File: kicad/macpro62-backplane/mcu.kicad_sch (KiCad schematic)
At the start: 0 parts

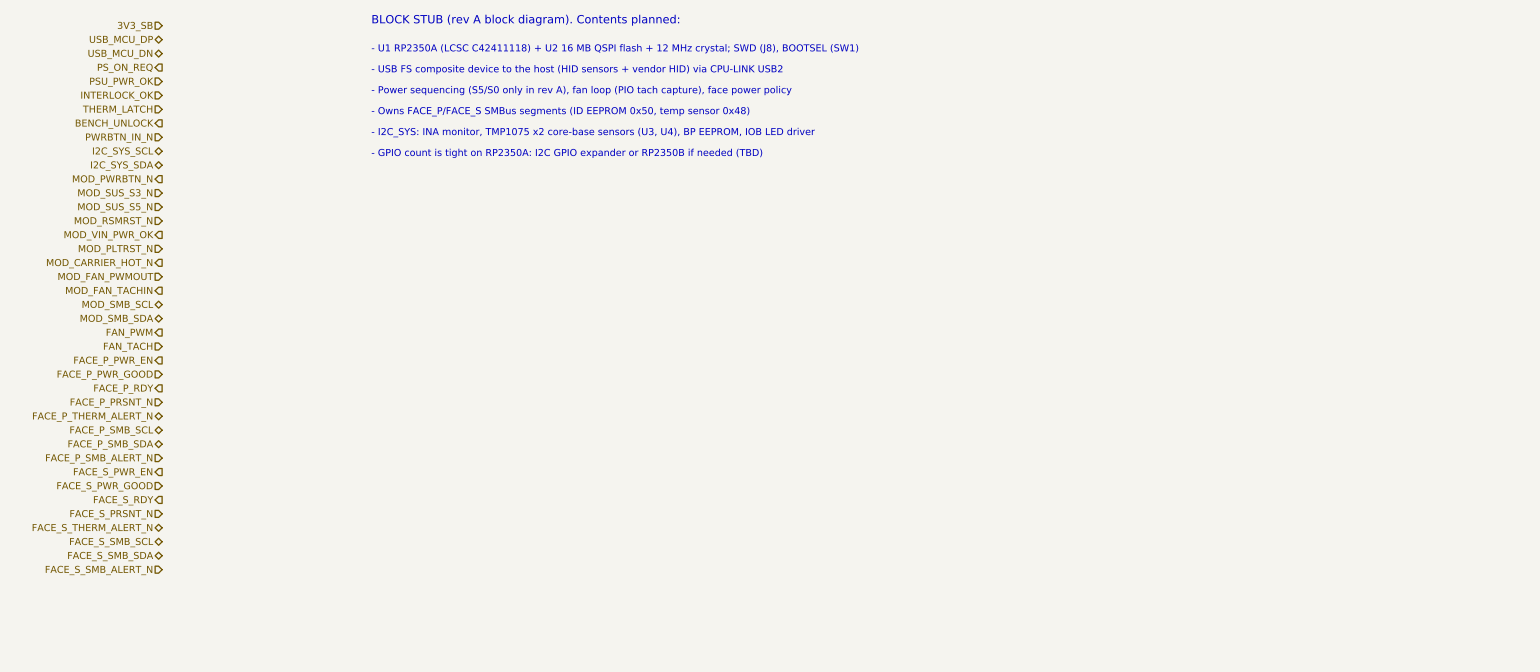
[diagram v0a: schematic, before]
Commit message: Cross-board compatibility audit: interface control doc, CR-BP-1 applied, J2/J3 row-swap pinouts, 15-pin face AUX, fan header removed from backplane, CPU board i226/BT1 cleanup
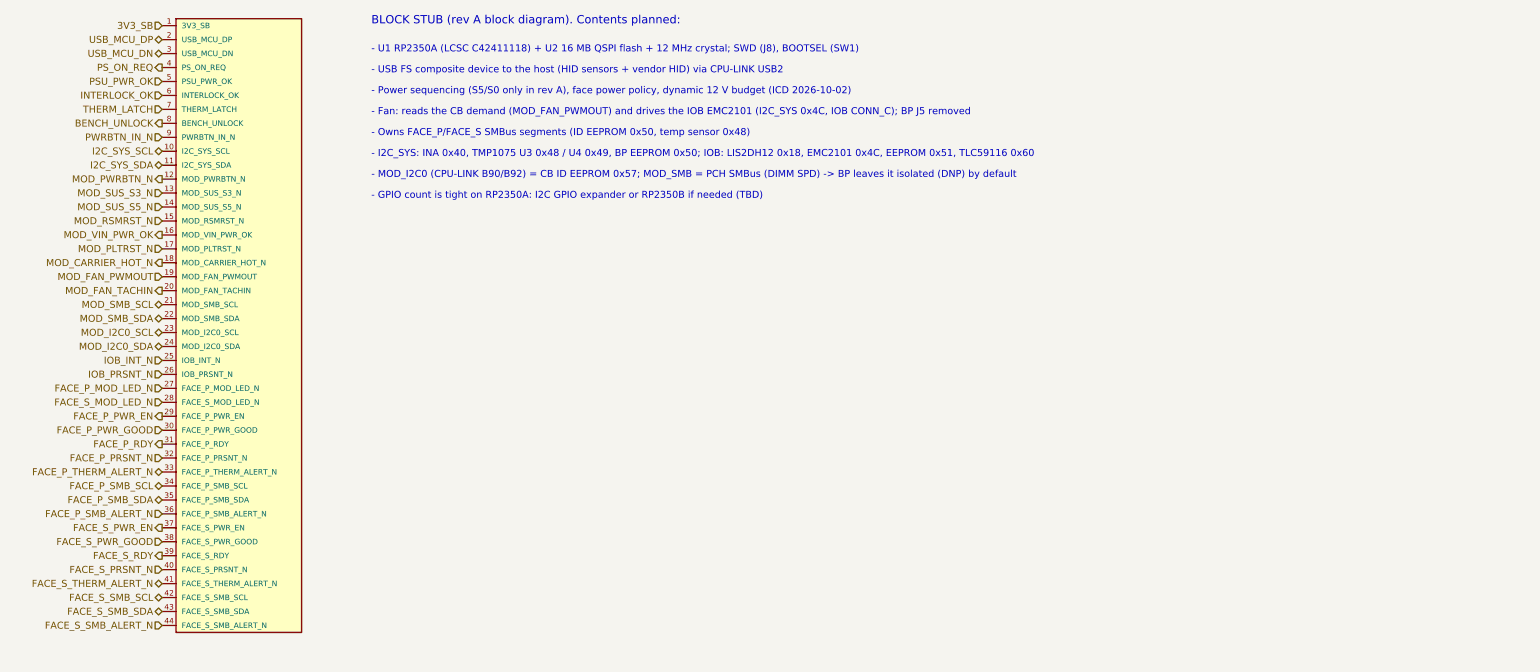
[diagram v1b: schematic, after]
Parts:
- added #BLK2: STUB_MCU, symbol MP62:STUB_MCU
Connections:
- net 3V3_SB: now also #BLK2.1 (3V3_SB)
- net BENCH_UNLOCK: now also #BLK2.8 (BENCH_UNLOCK)
- net FACE_P_PRSNT_N: now also #BLK2.32 (FACE_P_PRSNT_N)
- net FACE_P_PWR_EN: now also #BLK2.29 (FACE_P_PWR_EN)
- net FACE_P_PWR_GOOD: now also #BLK2.30 (FACE_P_PWR_GOOD)
- net FACE_P_RDY: now also #BLK2.31 (FACE_P_RDY)
- net FACE_P_SMB_ALERT_N: now also #BLK2.36 (FACE_P_SMB_ALERT_N)
- net FACE_P_SMB_SCL: now also #BLK2.34 (FACE_P_SMB_SCL)
- net FACE_P_SMB_SDA: now also #BLK2.35 (FACE_P_SMB_SDA)
- net FACE_P_THERM_ALERT_N: now also #BLK2.33 (FACE_P_THERM_ALERT_N)
- net FACE_S_PRSNT_N: now also #BLK2.40 (FACE_S_PRSNT_N)
- net FACE_S_PWR_EN: now also #BLK2.37 (FACE_S_PWR_EN)
- net FACE_S_PWR_GOOD: now also #BLK2.38 (FACE_S_PWR_GOOD)
- net FACE_S_RDY: now also #BLK2.39 (FACE_S_RDY)
- net FACE_S_SMB_ALERT_N: now also #BLK2.44 (FACE_S_SMB_ALERT_N)
- net FACE_S_SMB_SCL: now also #BLK2.42 (FACE_S_SMB_SCL)
- net FACE_S_SMB_SDA: now also #BLK2.43 (FACE_S_SMB_SDA)
- net FACE_S_THERM_ALERT_N: now also #BLK2.41 (FACE_S_THERM_ALERT_N)
- net I2C_SYS_SCL: now also #BLK2.10 (I2C_SYS_SCL)
- net I2C_SYS_SDA: now also #BLK2.11 (I2C_SYS_SDA)
- net INTERLOCK_OK: now also #BLK2.6 (INTERLOCK_OK)
- net MOD_CARRIER_HOT_N: now also #BLK2.18 (MOD_CARRIER_HOT_N)
- net MOD_FAN_PWMOUT: now also #BLK2.19 (MOD_FAN_PWMOUT)
- net MOD_FAN_TACHIN: now also #BLK2.20 (MOD_FAN_TACHIN)
- net MOD_PLTRST_N: now also #BLK2.17 (MOD_PLTRST_N)
- net MOD_PWRBTN_N: now also #BLK2.12 (MOD_PWRBTN_N)
- net MOD_RSMRST_N: now also #BLK2.15 (MOD_RSMRST_N)
- net MOD_SMB_SCL: now also #BLK2.21 (MOD_SMB_SCL)
- net MOD_SMB_SDA: now also #BLK2.22 (MOD_SMB_SDA)
- net MOD_SUS_S3_N: now also #BLK2.13 (MOD_SUS_S3_N)
- net MOD_SUS_S5_N: now also #BLK2.14 (MOD_SUS_S5_N)
- net MOD_VIN_PWR_OK: now also #BLK2.16 (MOD_VIN_PWR_OK)
- net PSU_PWR_OK: now also #BLK2.5 (PSU_PWR_OK)
- net PS_ON_REQ: now also #BLK2.4 (PS_ON_REQ)
- net PWRBTN_IN_N: now also #BLK2.9 (PWRBTN_IN_N)
- net THERM_LATCH: now also #BLK2.7 (THERM_LATCH)
- net USB_MCU_DN: now also #BLK2.3 (USB_MCU_DN)
- net USB_MCU_DP: now also #BLK2.2 (USB_MCU_DP)
- new net FACE_P_MOD_LED_N: #BLK2.27 (FACE_P_MOD_LED_N)
- new net FACE_S_MOD_LED_N: #BLK2.28 (FACE_S_MOD_LED_N)
- new net IOB_INT_N: #BLK2.25 (IOB_INT_N)
- new net IOB_PRSNT_N: #BLK2.26 (IOB_PRSNT_N)
- new net MOD_I2C0_SCL: #BLK2.23 (MOD_I2C0_SCL)
- new net MOD_I2C0_SDA: #BLK2.24 (MOD_I2C0_SDA)
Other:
- note added: "- Fan: reads the CB demand (MOD_FAN_PWMOUT) and drives the IOB EMC2101 (I2C_SYS 0x4C, IOB CONN_C); BP J5 removed"
- note added: "- I2C_SYS: INA 0x40, TMP1075 U3 0x48 / U4 0x49, BP EEPROM 0x50; IOB: LIS2DH12 0x18, EMC2101 0x4C, EEPROM 0x51, TLC59116 0x60"
- note added: "- MOD_I2C0 (CPU-LINK B90/B92) = CB ID EEPROM 0x57; MOD_SMB = PCH SMBus (DIMM SPD) -> BP leaves it isolated (DNP) by default"
- note added: "- Power sequencing (S5/S0 only in rev A), face power policy, dynamic 12 V budget (ICD 2026-10-02)"
- note removed: "- I2C_SYS: INA monitor, TMP1075 x2 core-base sensors (U3, U4), BP EEPROM, IOB LED driver"
- note removed: "- Power sequencing (S5/S0 only in rev A), fan loop (PIO tach capture), face power policy"
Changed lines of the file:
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@@
 	(title_block
 		(title "MP62 backplane: Management MCU (RP2350A)")
-		(date "2026-10-01")
-		(rev "A-bd1")
-		(comment 1 "Block stub: hierarchical labels only, circuit TBD")
+		(date "2026-10-02")
+		(rev "A-bd2")
+		(comment 1 "Block stub: hierarchical labels + one non-BOM stub symbol (#BLKn, passive pins) so ERC sees the nets; circuit TBD")
 	)
 	(hierarchical_label "3V3_SB"
@@
 		(effects (font (size 1.27 1.27)) (justify right))
 	)
-	(hierarchical_label "FAN_PWM"
-		(shape output)
+	(hierarchical_label "MOD_I2C0_SCL"
+		(shape bidirectional)
 		(at 38.1 86.36 180)
 		(effects (font (size 1.27 1.27)) (justify right))
 	)
-	(hierarchical_label "FAN_TACH"
-		(shape input)
+	(hierarchical_label "MOD_I2C0_SDA"
+		(shape bidirectional)
 		(at 38.1 88.90 180)
 		(effects (font (size 1.27 1.27)) (justify right))
 	)
+	(hierarchical_label "IOB_INT_N"
+		(shape input)
+		(at 38.1 91.44 180)
+		(effects (font (size 1.27 1.27)) (justify right))
+	)
+	(hierarchical_label "IOB_PRSNT_N"
+		(shape input)
+		(at 38.1 93.98 180)
+		(effects (font (size 1.27 1.27)) (justify right))
+	)
+	(hierarchical_label "FACE_P_MOD_LED_N"
+		(shape input)
+		(at 38.1 96.52 180)
+		(effects (font (size 1.27 1.27)) (justify right))
+	)
+	(hierarchical_label "FACE_S_MOD_LED_N"
+		(shape input)
+		(at 38.1 99.06 180)
+		(effects (font (size 1.27 1.27)) (justify right))
+	)
 	(hierarchical_label "FACE_P_PWR_EN"
 		(shape output)
-		(at 38.1 91.44 180)
+		(at 38.1 101.60 180)
 		(effects (font (size 1.27 1.27)) (justify right))
 	)
 	(hierarchical_label "FACE_P_PWR_GOOD"
 		(shape input)
-		(at 38.1 93.98 180)
+		(at 38.1 104.14 180)
 		(effects (font (size 1.27 1.27)) (justify right))
 	)
 	(hierarchical_label "FACE_P_RDY"
 		(shape output)
-		(at 38.1 96.52 180)
+		(at 38.1 106.68 180)
 		(effects (font (size 1.27 1.27)) (justify right))
 	)
 	(hierarchical_label "FACE_P_PRSNT_N"
 		(shape input)
-		(at 38.1 99.06 180)
+		(at 38.1 109.22 180)
 		(effects (font (size 1.27 1.27)) (justify right))
 	)
 	(hierarchical_label "FACE_P_THERM_ALERT_N"
 		(shape bidirectional)
-		(at 38.1 101.60 180)
+		(at 38.1 111.76 180)
 		(effects (font (size 1.27 1.27)) (justify right))
 	)
 	(hierarchical_label "FACE_P_SMB_SCL"
 		(shape bidirectional)
-		(at 38.1 104.14 180)
+		(at 38.1 114.30 180)
 		(effects (font (size 1.27 1.27)) (justify right))
 	)
 	(hierarchical_label "FACE_P_SMB_SDA"
 		(shape bidirectional)
-		(at 38.1 106.68 180)
+		(at 38.1 116.84 180)
 		(effects (font (size 1.27 1.27)) (justify right))
 	)
 	(hierarchical_label "FACE_P_SMB_ALERT_N"
 		(shape input)
-		(at 38.1 109.22 180)
+		(at 38.1 119.38 180)
 		(effects (font (size 1.27 1.27)) (justify right))
 	)
 	(hierarchical_label "FACE_S_PWR_EN"
 		(shape output)
-		(at 38.1 111.76 180)
+		(at 38.1 121.92 180)
 		(effects (font (size 1.27 1.27)) (justify right))
 	)
 	(hierarchical_label "FACE_S_PWR_GOOD"
 		(shape input)
-		(at 38.1 114.30 180)
+		(at 38.1 124.46 180)
 		(effects (font (size 1.27 1.27)) (justify right))
 	)
 	(hierarchical_label "FACE_S_RDY"
 		(shape output)
-		(at 38.1 116.84 180)
+		(at 38.1 127.00 180)
 		(effects (font (size 1.27 1.27)) (justify right))
 	)
 	(hierarchical_label "FACE_S_PRSNT_N"
 		(shape input)
-		(at 38.1 119.38 180)
+		(at 38.1 129.54 180)
 		(effects (font (size 1.27 1.27)) (justify right))
 	)
 	(hierarchical_label "FACE_S_THERM_ALERT_N"
 		(shape bidirectional)
-		(at 38.1 121.92 180)
+		(at 38.1 132.08 180)
 		(effects (font (size 1.27 1.27)) (justify right))
 	)
 	(hierarchical_label "FACE_S_SMB_SCL"
 		(shape bidirectional)
-		(at 38.1 124.46 180)
+		(at 38.1 134.62 180)
 		(effects (font (size 1.27 1.27)) (justify right))
 	)
 	(hierarchical_label "FACE_S_SMB_SDA"
 		(shape bidirectional)
-		(at 38.1 127.00 180)
+		(at 38.1 137.16 180)
 		(effects (font (size 1.27 1.27)) (justify right))
 	)
 	(hierarchical_label "FACE_S_SMB_ALERT_N"
 		(shape input)
-		(at 38.1 129.54 180)
-		(effects (font (size 1.27 1.27)) (justify right))
+		(at 38.1 139.70 180)
+		(effects (font (size 1.27 1.27)) (justify right))
+	)
+	(symbol
+		(lib_id "MP62:STUB_MCU")
+		(at 38.1 30.48 0)
+		(unit 1)
+		(exclude_from_sim yes)
+		(in_bom no)
+		(on_board no)
+		(dnp no)
+		(property "Reference" "#BLK2"
+			(at 40.64 27.94 0)
+			(effects (font (size 1.27 1.27)) (justify left) (hide yes))
+		)
+		(property "Value" "STUB_MCU"
+			(at 40.64 26.67 0)
+			(effects (font (size 1.27 1.27)) (justify left) (hide yes))
+		)
+		(pin "1"
+		)
+		(pin "2"
+		)
+		(pin "3"
+		)
+		(pin "4"
+		)
+		(pin "5"
+		)
+		(pin "6"
+		)
+		(pin "7"
+		)
+		(pin "8"
+		)
+		(pin "9"
+		)
+		(pin "10"
+		)
+		(pin "11"
+		)
+		(pin "12"
+		)
+		(pin "13"
+		)
+		(pin "14"
+		)
+		(pin "15"
+		)
+		(pin "16"
+		)
+		(pin "17"
+		)
+		(pin "18"
+		)
+		(pin "19"
+		)
+		(pin "20"
+		)
+		(pin "21"
+		)
+		(pin "22"
+		)
+		(pin "23"
+		)
+		(pin "24"
+		)
+		(pin "25"
+		)
+		(pin "26"
+		)
+		(pin "27"
+		)
+		(pin "28"
+		)
+		(pin "29"
+		)
+		(pin "30"
+		)
+		(pin "31"
+		)
+		(pin "32"
+		)
+		(pin "33"
+		)
+		(pin "34"
+		)
+		(pin "35"
+		)
+		(pin "36"
+		)
+		(pin "37"
+		)
+		(pin "38"
+		)
+		(pin "39"
+		)
+		(pin "40"
+		)
+		(pin "41"
+		)
+		(pin "42"
+		)
+		(pin "43"
+		)
+		(pin "44"
+		)
+		(instances
+			(project "backplane"
+				(path "/6a1c2d3e-0000-4000-8000-000000000062/89d03002-a1b1-4403-bf24-5238af15a71b"
+					(reference "#BLK2")
+					(unit 1)
+				)
+			)
+		)
 	)
 	(text "BLOCK STUB (rev A block diagram). Contents planned:"
@@
 		(effects (font (size 1.27 1.27)) (justify left bottom))
 	)
-	(text "- Power sequencing (S5/S0 only in rev A), fan loop (PIO tach capture), face power policy"
+	(text "- Power sequencing (S5/S0 only in rev A), face power policy, dynamic 12 V budget (ICD 2026-10-02)"
 		(exclude_from_sim no)
 		(at 76.20 43.18 0)
 		(effects (font (size 1.27 1.27)) (justify left bottom))
 	)
+	(text "- Fan: reads the CB demand (MOD_FAN_PWMOUT) and drives the IOB EMC2101 (I2C_SYS 0x4C, IOB CONN_C); BP J5 removed"
+		(exclude_from_sim no)
+		(at 76.20 46.99 0)
+		(effects (font (size 1.27 1.27)) (justify left bottom))
+	)
 	(text "- Owns FACE_P/FACE_S SMBus segments (ID EEPROM 0x50, temp sensor 0x48)"
 		(exclude_from_sim no)
-		(at 76.20 46.99 0)
-		(effects (font (size 1.27 1.27)) (justify left bottom))
-	)
-	(text "- I2C_SYS: INA monitor, TMP1075 x2 core-base sensors (U3, U4), BP EEPROM, IOB LED driver"
-		(exclude_from_sim no)
 		(at 76.20 50.80 0)
 		(effects (font (size 1.27 1.27)) (justify left bottom))
 	)
+	(text "- I2C_SYS: INA 0x40, TMP1075 U3 0x48 / U4 0x49, BP EEPROM 0x50; IOB: LIS2DH12 0x18, EMC2101 0x4C, EEPROM 0x51, TLC59116 0x60"
+		(exclude_from_sim no)
+		(at 76.20 54.61 0)
+		(effects (font (size 1.27 1.27)) (justify left bottom))
+	)
+	(text "- MOD_I2C0 (CPU-LINK B90/B92) = CB ID EEPROM 0x57; MOD_SMB = PCH SMBus (DIMM SPD) -> BP leaves it isolated (DNP) by default"
+		(exclude_from_sim no)
+		(at 76.20 58.42 0)
+		(effects (font (size 1.27 1.27)) (justify left bottom))
+	)
 	(text "- GPIO count is tight on RP2350A: I2C GPIO expander or RP2350B if needed (TBD)"
 		(exclude_from_sim no)
-		(at 76.20 54.61 0)
-		(effects (font (size 1.27 1.27)) (justify left bottom))
-	)
+		(at 76.20 62.23 0)
+		(effects (font (size 1.27 1.27)) (justify left bottom))
+	)
